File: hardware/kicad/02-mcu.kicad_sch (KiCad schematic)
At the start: 6 parts, among them SW14 BOOT, SW15 RESET, U1 ESP32-S3-N16R8

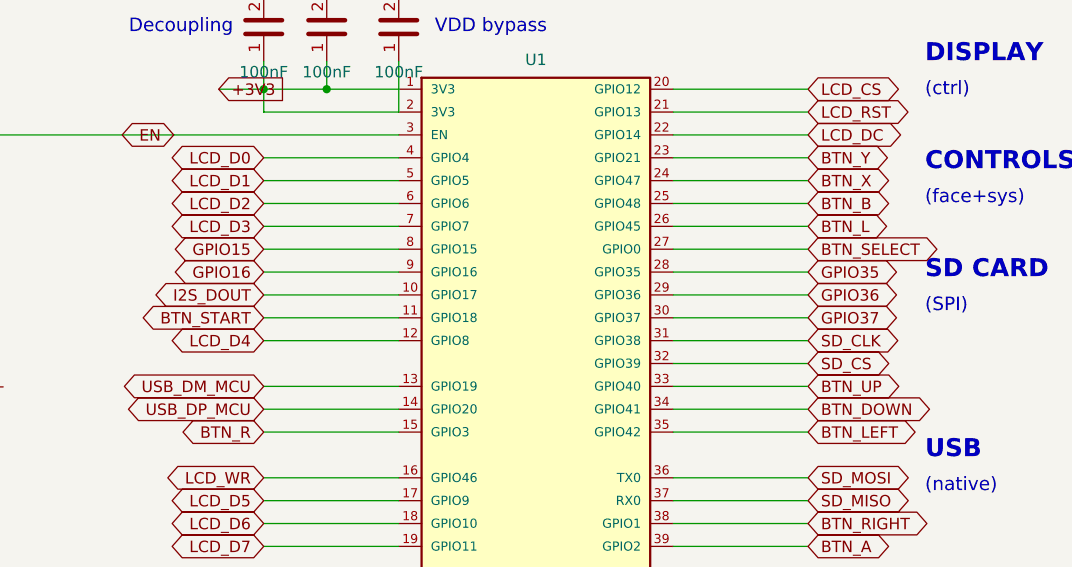
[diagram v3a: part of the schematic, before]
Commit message: refactor(schematics): zero dead nets, T1_ALLOW empty, legacy AMS1117 removed
Dead-net sweep requested by the user, both sides checked:

- PCB: already clean — 54 declared nets, 54 carrying copper (ORPHAN
  e-test gate enforces it). Nothing to do.
- Schematic: the five one-pin "GPIOnn" phantom nets (GPIO15/16/35/36/37)
  are now explicit no_connect markers. GPIO35-37 are the WROOM-1
  on-module PSRAM pins that MUST stay externally unconnected; 15/16 were
  freed when audio went PDM-DOUT-only (R10-LOW-2). T1_ALLOW is now
  EMPTY — five more allowlist holes closed, after LX/RPP_GATE earlier
  today: seven total, each one a node the schematic<->PCB cross-check
  now actually compares.
- Dangling BAT_IN stub next to J3 deleted: its wire started at
  jst_x+3.81 where J3 has no pin (both pins are on the connector's left
  side) — flagged by ERC as unconnected_wire_endpoint since forever.
- VBUS / BAT+ / BAT_IN no longer mix local and global labels on one net
  (ERC same_local_global_label): global labels only, so net merging no
  longer relies on KiCad's same-text courtesy.
- lib_symbols: legacy AMS1117-3.3 symbol removed (unused since the
  SY8089 swap; its stray power_out pins were noise in pin-type audits).

Docs: ecosystem-analysis updated (dead-net sweep + empty T1_ALLOW).
Deferred deep-dives recorded in memory: SW16 shell-isolation datasheet
check, 636 remaining ERC warnings, netlist cosmetic warning.

Tests: verify-all 80/80, verify-erc PASS (0 errors; warnings 651->636),
netlist-diff 4/4 with T1_ALLOW=∅, overlaps 651 items clean,
label-attach 131/131, verify-memory 6/6, website-build green.
Schematic SVG/PDF renders + combined PDF regenerated.

Co-Authored-By: Claude Fable 5 <noreply@anthropic.com>
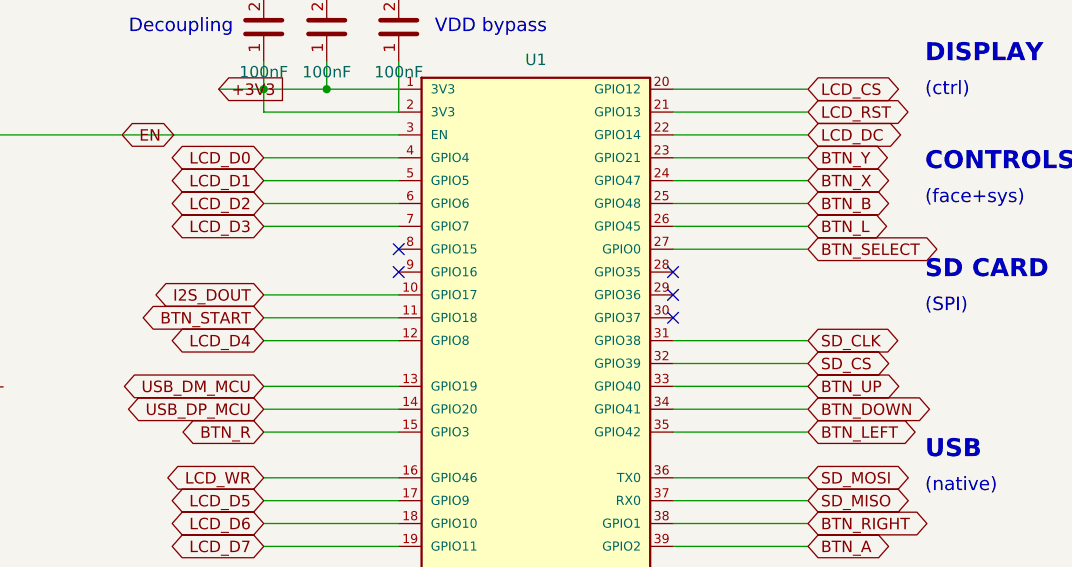
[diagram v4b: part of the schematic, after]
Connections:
- net GPIO15: no longer names the net of U1.8 (GPIO15)
- net GPIO16: no longer names the net of U1.9 (GPIO16)
- net GPIO35: no longer names the net of U1.28 (GPIO35)
- net GPIO36: no longer names the net of U1.29 (GPIO36)
- net GPIO37: no longer names the net of U1.30 (GPIO37)
- no-connect marks 0 -> 5
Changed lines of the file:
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@@
   (wire (pts (xy 184.76 147.14) (xy 169.76 147.14)) (stroke (width 0) (type default)))
   (global_label "LCD_D3" (shape bidirectional) (at 169.76 147.14 180) (effects (font (size 1.27 1.27))) (property "Intersheetrefs" "" (at 0 0 0) (effects (font (size 1.27 1.27)) hide)))
-  (wire (pts (xy 184.76 149.68) (xy 169.76 149.68)) (stroke (width 0) (type default)))
-  (global_label "GPIO15" (shape bidirectional) (at 169.76 149.68 180) (effects (font (size 1.27 1.27))) (property "Intersheetrefs" "" (at 0 0 0) (effects (font (size 1.27 1.27)) hide)))
-  (wire (pts (xy 184.76 152.22) (xy 169.76 152.22)) (stroke (width 0) (type default)))
-  (global_label "GPIO16" (shape bidirectional) (at 169.76 152.22 180) (effects (font (size 1.27 1.27))) (property "Intersheetrefs" "" (at 0 0 0) (effects (font (size 1.27 1.27)) hide)))
+  (no_connect (at 184.76 149.68))
+  (no_connect (at 184.76 152.22))
   (wire (pts (xy 184.76 154.76) (xy 169.76 154.76)) (stroke (width 0) (type default)))
   (global_label "I2S_DOUT" (shape bidirectional) (at 169.76 154.76 180) (effects (font (size 1.27 1.27))) (property "Intersheetrefs" "" (at 0 0 0) (effects (font (size 1.27 1.27)) hide)))
@@
   (wire (pts (xy 215.24 149.68) (xy 230.24 149.68)) (stroke (width 0) (type default)))
   (global_label "BTN_SELECT" (shape bidirectional) (at 230.24 149.68 0) (effects (font (size 1.27 1.27))) (property "Intersheetrefs" "" (at 0 0 0) (effects (font (size 1.27 1.27)) hide)))
-  (wire (pts (xy 215.24 152.22) (xy 230.24 152.22)) (stroke (width 0) (type default)))
-  (global_label "GPIO35" (shape bidirectional) (at 230.24 152.22 0) (effects (font (size 1.27 1.27))) (property "Intersheetrefs" "" (at 0 0 0) (effects (font (size 1.27 1.27)) hide)))
-  (wire (pts (xy 215.24 154.76) (xy 230.24 154.76)) (stroke (width 0) (type default)))
-  (global_label "GPIO36" (shape bidirectional) (at 230.24 154.76 0) (effects (font (size 1.27 1.27))) (property "Intersheetrefs" "" (at 0 0 0) (effects (font (size 1.27 1.27)) hide)))
-  (wire (pts (xy 215.24 157.3) (xy 230.24 157.3)) (stroke (width 0) (type default)))
-  (global_label "GPIO37" (shape bidirectional) (at 230.24 157.3 0) (effects (font (size 1.27 1.27))) (property "Intersheetrefs" "" (at 0 0 0) (effects (font (size 1.27 1.27)) hide)))
+  (no_connect (at 215.24 152.22))
+  (no_connect (at 215.24 154.76))
+  (no_connect (at 215.24 157.3))
   (wire (pts (xy 215.24 159.84) (xy 230.24 159.84)) (stroke (width 0) (type default)))
   (global_label "SD_CLK" (shape bidirectional) (at 230.24 159.84 0) (effects (font (size 1.27 1.27))) (property "Intersheetrefs" "" (at 0 0 0) (effects (font (size 1.27 1.27)) hide)))
